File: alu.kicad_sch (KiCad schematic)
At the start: 31 parts, among them SW0 SW_DIP_x04, SW1 SW_DIP_x04, SW3 SW_DIP_x04, U1 SN74HC86N, U10 SN74LS08N, U2 SN74LS08N, U3 CD74HCT32E, U4 SN74HC86N, U5 SN74LS08N

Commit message: feat: updated footprint
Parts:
- R0, R1, R12, R2, R3: footprint (none) -> Resistor_SMD:R_2512_6332Metric_Pad1.40x3.35mm_HandSolder
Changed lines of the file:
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@@
 			)
 		)
-		(property "Footprint" ""
+		(property "Footprint" "Resistor_SMD:R_2512_6332Metric_Pad1.40x3.35mm_HandSolder"
 			(at 252.73 138.938 90)
 			(hide yes)
@@
 			)
 		)
-		(property "Footprint" ""
+		(property "Footprint" "Resistor_SMD:R_2512_6332Metric_Pad1.40x3.35mm_HandSolder"
 			(at 252.73 151.638 90)
 			(hide yes)
@@
 			)
 		)
-		(property "Footprint" ""
+		(property "Footprint" "Resistor_SMD:R_2512_6332Metric_Pad1.40x3.35mm_HandSolder"
 			(at 252.73 145.288 90)
 			(hide yes)
@@
 			)
 		)
-		(property "Footprint" ""
+		(property "Footprint" "Resistor_SMD:R_2512_6332Metric_Pad1.40x3.35mm_HandSolder"
 			(at 251.46 160.528 90)
 			(hide yes)
@@
 			)
 		)
-		(property "Footprint" ""
+		(property "Footprint" "Resistor_SMD:R_2512_6332Metric_Pad1.40x3.35mm_HandSolder"
 			(at 252.73 132.588 90)
 			(hide yes)

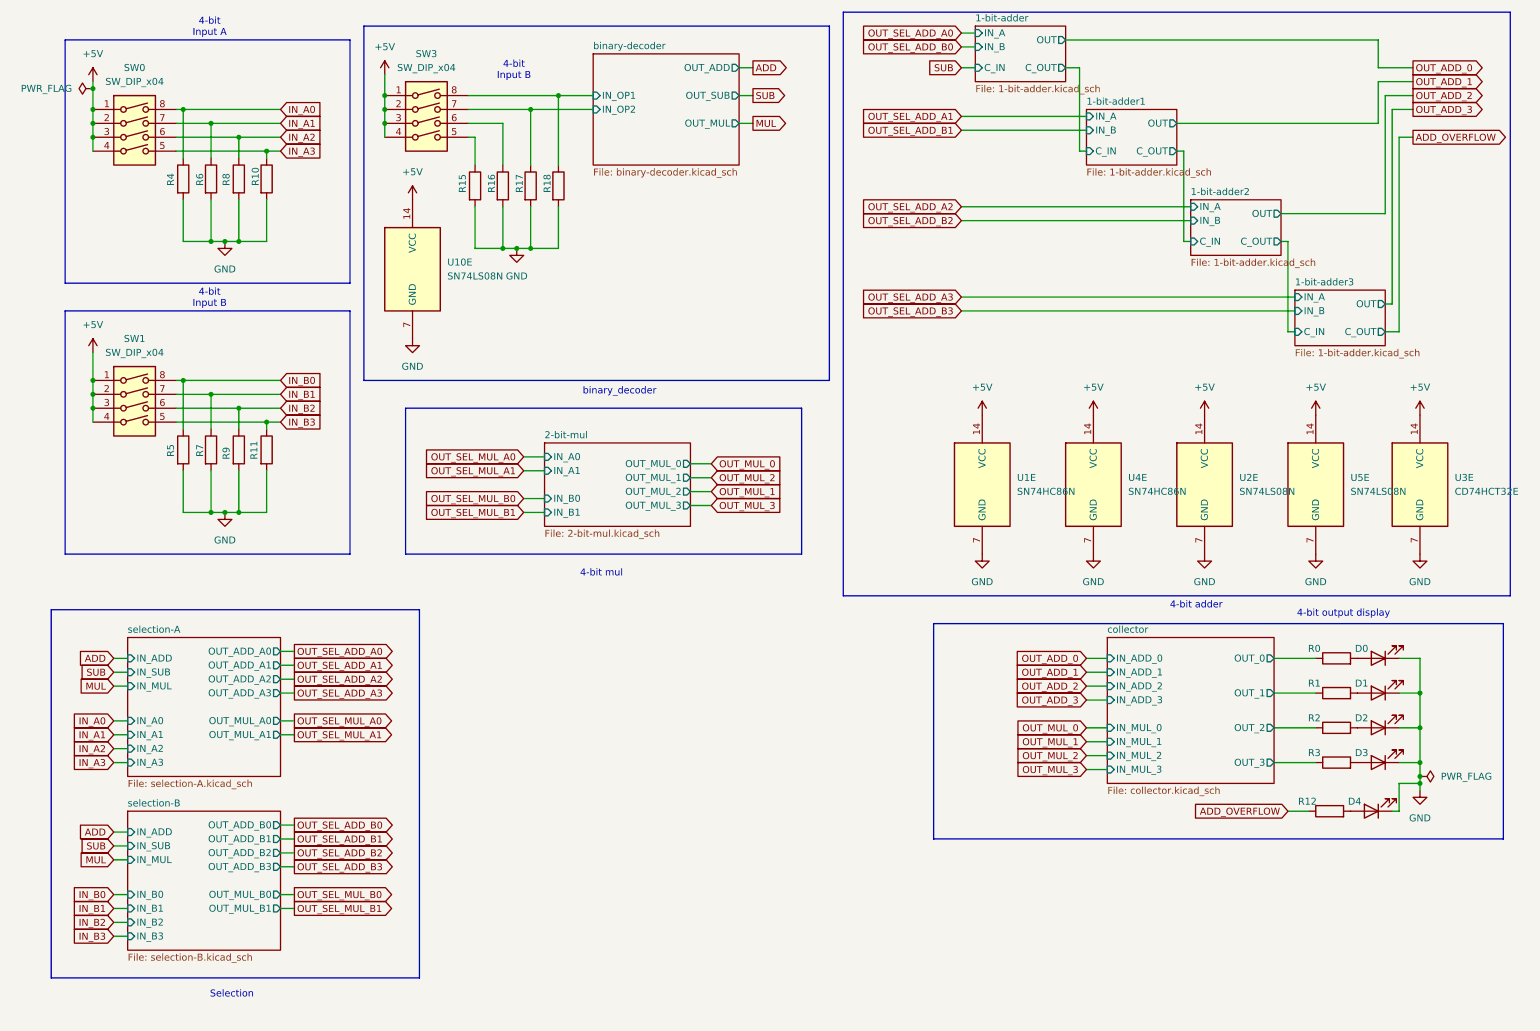
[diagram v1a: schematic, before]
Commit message: feat: usb c
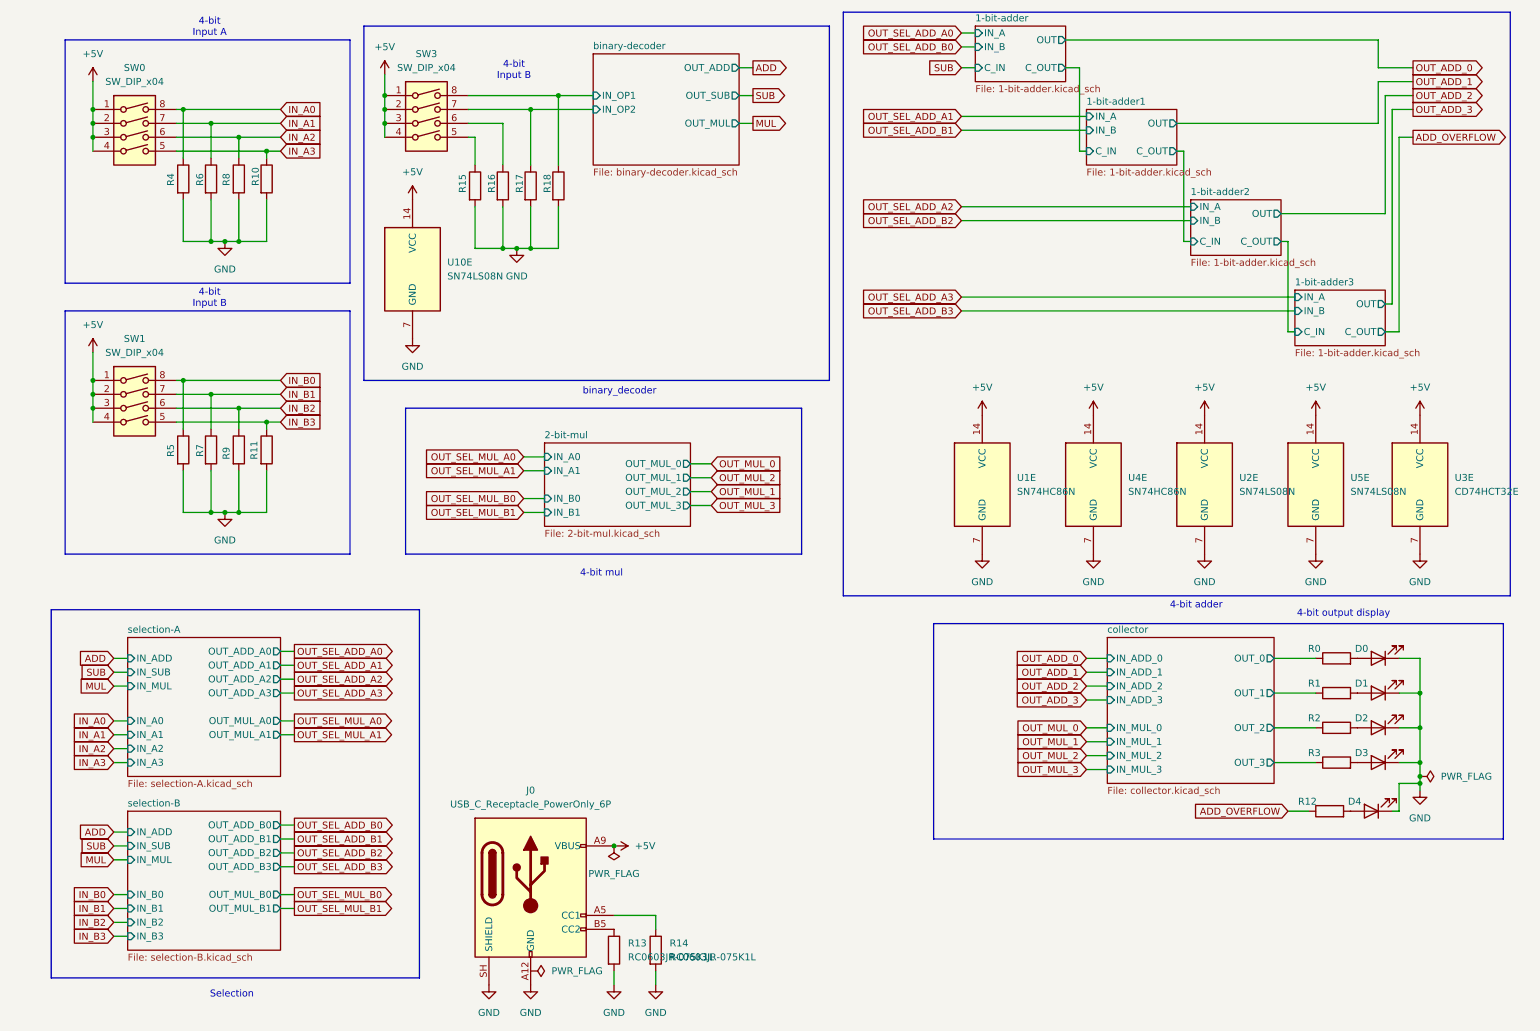
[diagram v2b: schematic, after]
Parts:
- added J0: USB_C_Receptacle_PowerOnly_6P, symbol Connector:USB_C_Receptacle_PowerOnly_6P
- added R13, R14: RC0603JR-075K1L, Resistor_SMD:R_0201_0603Metric_Pad0.64x0.40mm_HandSolder, symbol Device:R
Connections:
- net +5V: now also J0.A9 (VBUS), J0.B9 (VBUS)
- net GND: now also J0.A12 (GND), J0.B12 (GND), J0.SH (SHIELD), R13.2, R14.2
- new net: J0.A5 (CC1), R14.1
- new net: J0.B5 (CC2), R13.1

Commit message: fix: forgot to save before commit
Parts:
- SW0, SW1, SW3: footprint Package_DIP:DIP-4_W7.62mm -> Package_DIP:DIP-4_W7.62mm_LongPads
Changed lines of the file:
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@@
 			)
 		)
-		(property "Footprint" "Package_DIP:DIP-4_W7.62mm"
+		(property "Footprint" "Package_DIP:DIP-4_W7.62mm_LongPads"
 			(at 33.02 35.56 0)
 			(hide yes)
@@
 			)
 		)
-		(property "Footprint" "Package_DIP:DIP-4_W7.62mm"
+		(property "Footprint" "Package_DIP:DIP-4_W7.62mm_LongPads"
 			(at 86.36 33.02 0)
 			(hide yes)
@@
 			)
 		)
-		(property "Footprint" "Package_DIP:DIP-4_W7.62mm"
+		(property "Footprint" "Package_DIP:DIP-4_W7.62mm_LongPads"
 			(at 33.02 85.09 0)
 			(hide yes)

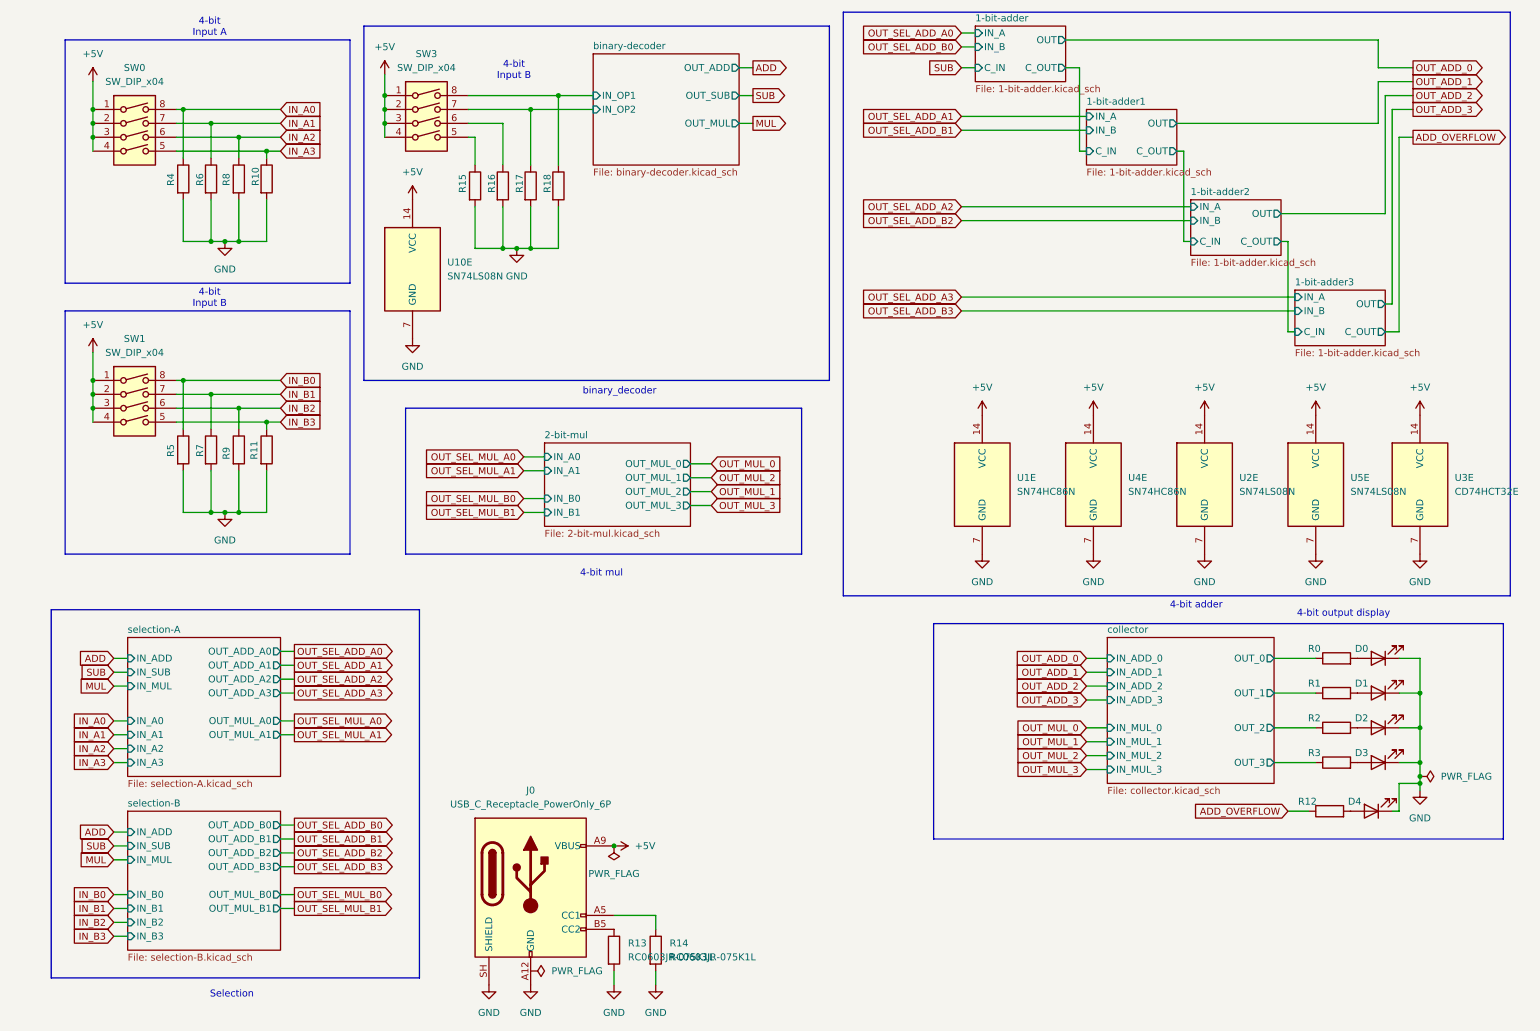
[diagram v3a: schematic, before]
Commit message: feat: added capacitor with footprint
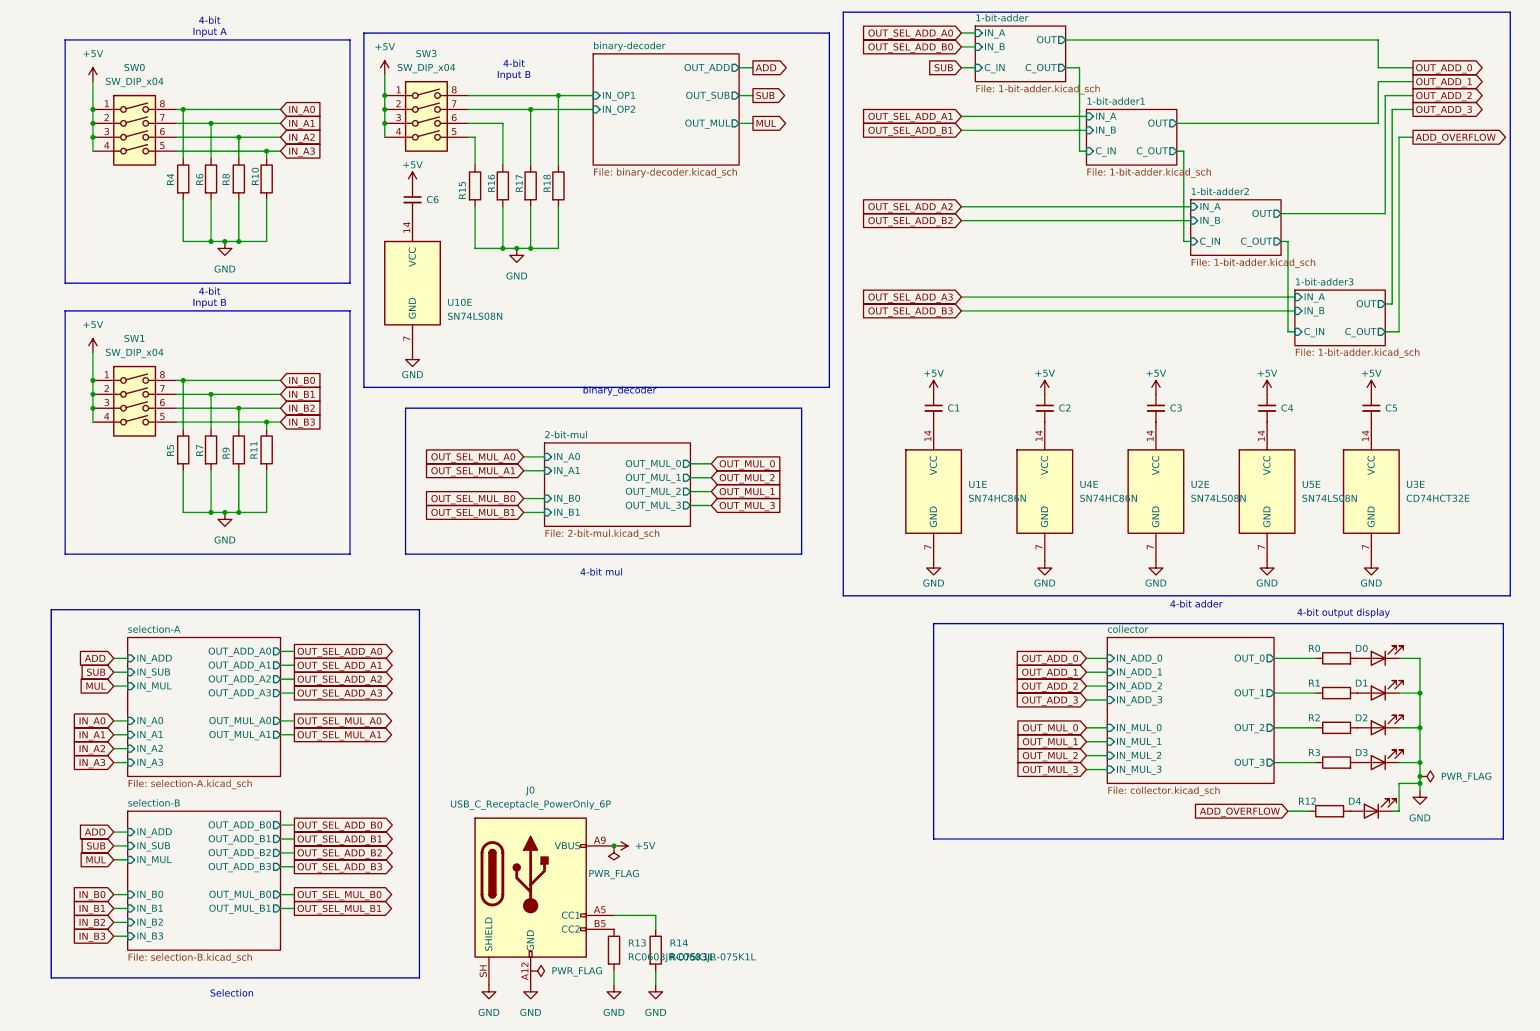
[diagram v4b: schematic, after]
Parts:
- added C1, C2, C3, C4, C5, C6: C_Small, Capacitor_SMD:C_0603_1608Metric_Pad1.08x0.95mm_HandSolder, symbol Device:C_Small
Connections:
- net +5V: now also C1.1, C2.1, C3.1, C4.1, C5.1, C6.1; no longer U1.14 (VCC), U10.14 (VCC), U2.14 (VCC), U3.14 (VCC), U4.14 (VCC), U5.14 (VCC)
- new net: C3.2, U2.14 (VCC)
- new net: C1.2, U1.14 (VCC)
- new net: C2.2, U4.14 (VCC)
- new net: C4.2, U5.14 (VCC)
- new net: C6.2, U10.14 (VCC)
- new net: C5.2, U3.14 (VCC)
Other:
- moved on the sheet: U10E, U1E, U2E, U3E, U4E, U5E

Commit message: feat: usb c
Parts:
- removed C1, C2: C_Small, Capacitor_SMD:C_0603_1608Metric_Pad1.08x0.95mm_HandSolder, symbol Device:C_Small
- added C0: 885012106031, Capacitor_SMD:C_0201_0603Metric_Pad0.64x0.40mm_HandSolder, symbol Device:C
- J0: value USB_C_Receptacle_PowerOnly_6P -> 640-USB4970-00-A; footprint (none) -> Connector_USB:USB_C_Receptacle_GCT_USB4125-xx-x_6P_TopMnt_Horizontal
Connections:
- net +5V: now also C0.1; no longer C3.1, C4.1, C5.1, C6.1
- net GND: now also C0.2
- net at U2.14 (VCC): no longer C3.2
- net at U5.14 (VCC): no longer C4.2
- net at U10.14 (VCC): no longer C6.2
- net at U3.14 (VCC): no longer C5.2
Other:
- note added: "Alimentation (USB-C)"
- moved on the sheet: J0, R13, R14

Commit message: fix: merge
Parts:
- added C0, C2: CC0603KRX7R9BB104, Capacitor_SMD:C_0603_1608Metric_Pad1.08x0.95mm_HandSolder, symbol Device:C_Small
- C3, C4, C5, C6: value C_Small -> CC0603KRX7R9BB104
- renumbered C0 to C1, D4 to D0, D0 to D1, D1 to D2, D2 to D3, D3 to D4, R4 to R0, R5 to R1, R17 to R10, R18 to R11, R13 to R12, R14 to R13, R12 to R14, R0 to R15, R1 to R16, R2 to R17, R3 to R18, R6 to R2, R7 to R3, R8 to R4, R9 to R5, R10 to R6, R11 to R7, R15 to R8, R16 to R9, SW3 to SW2, U10 to U0, U4 to U2, U2 to U3, U5 to U4, U3 to U5
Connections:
- net +5V: now also C3.1, C4.1, C5.1, C6.1, C0.1, C2.1
- net at U3.14 (VCC): now also C4.2
- net at U1.14 (VCC): now also C2.2
- net at U2.14 (VCC): now also C3.2
- net at U0.14 (VCC): now also C0.2
- net at U5.14 (VCC): now also C6.2
- net at U4.14 (VCC): now also C5.2

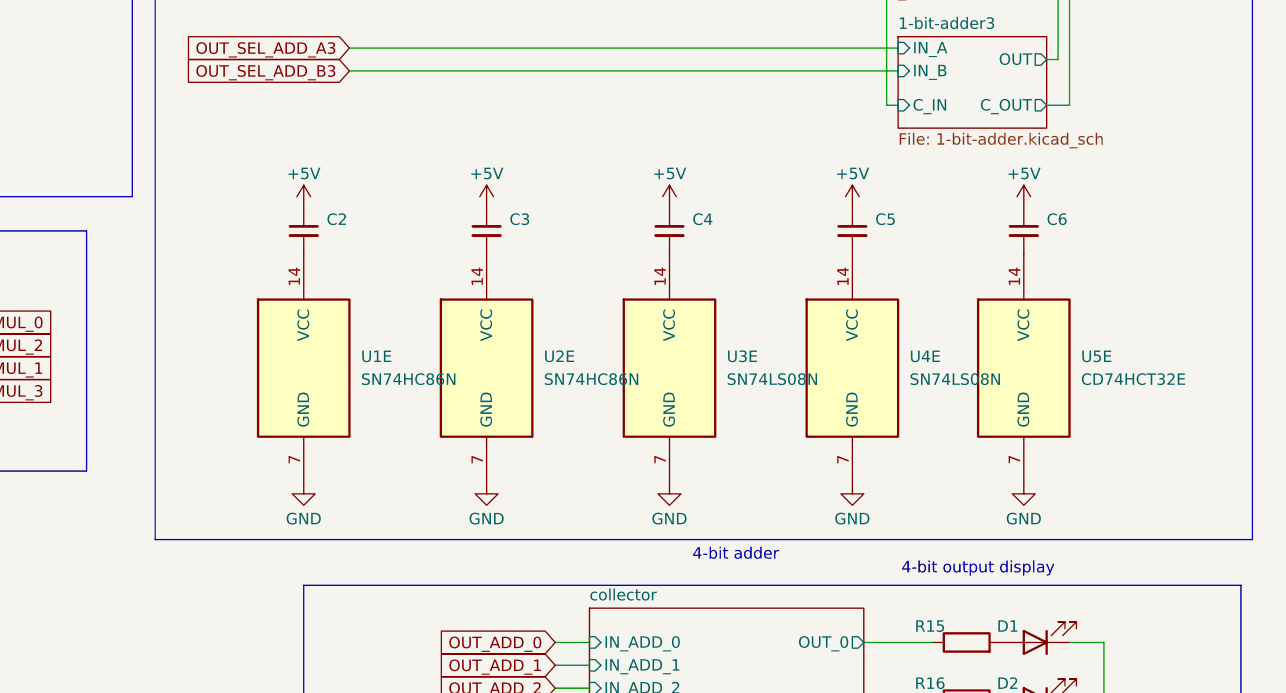
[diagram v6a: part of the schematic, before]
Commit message: fix: capacitor collector/add
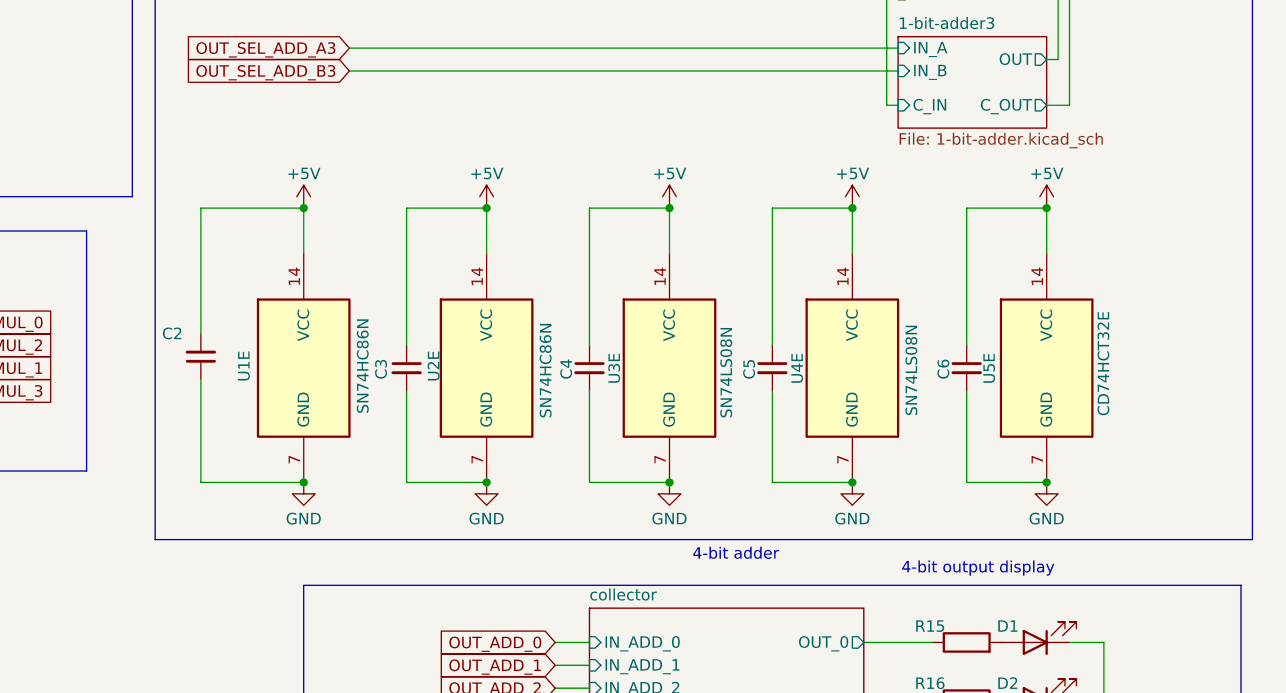
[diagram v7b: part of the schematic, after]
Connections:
- net +5V: now also C2.2, U1.14 (VCC), U2.14 (VCC), U3.14 (VCC), U4.14 (VCC), U5.14 (VCC); no longer C2.1
- net GND: now also C2.1, C3.2, C4.2, C5.2, C6.2
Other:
- moved on the sheet: C2, C3, C4, C5, C6, U5E
